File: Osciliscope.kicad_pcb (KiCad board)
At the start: 2 copper layers, 39.6 x 60.2 mm, 42 parts, among them J1 U.FL, J2 Conn_01x04_Socket, J3 U.FL, J4 Conn_01x04_Socket, J5 USB_C_Receptacle_USB2.0_14P, J6 Conn_01x02_MountingPin, SW1 SW_Rotary_1x8_MP, SW2 SW_Rotary_1x8_MP, SW3 SW_Nidec_CAS-120A1, SW4 SW_Nidec_CAS-120A1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

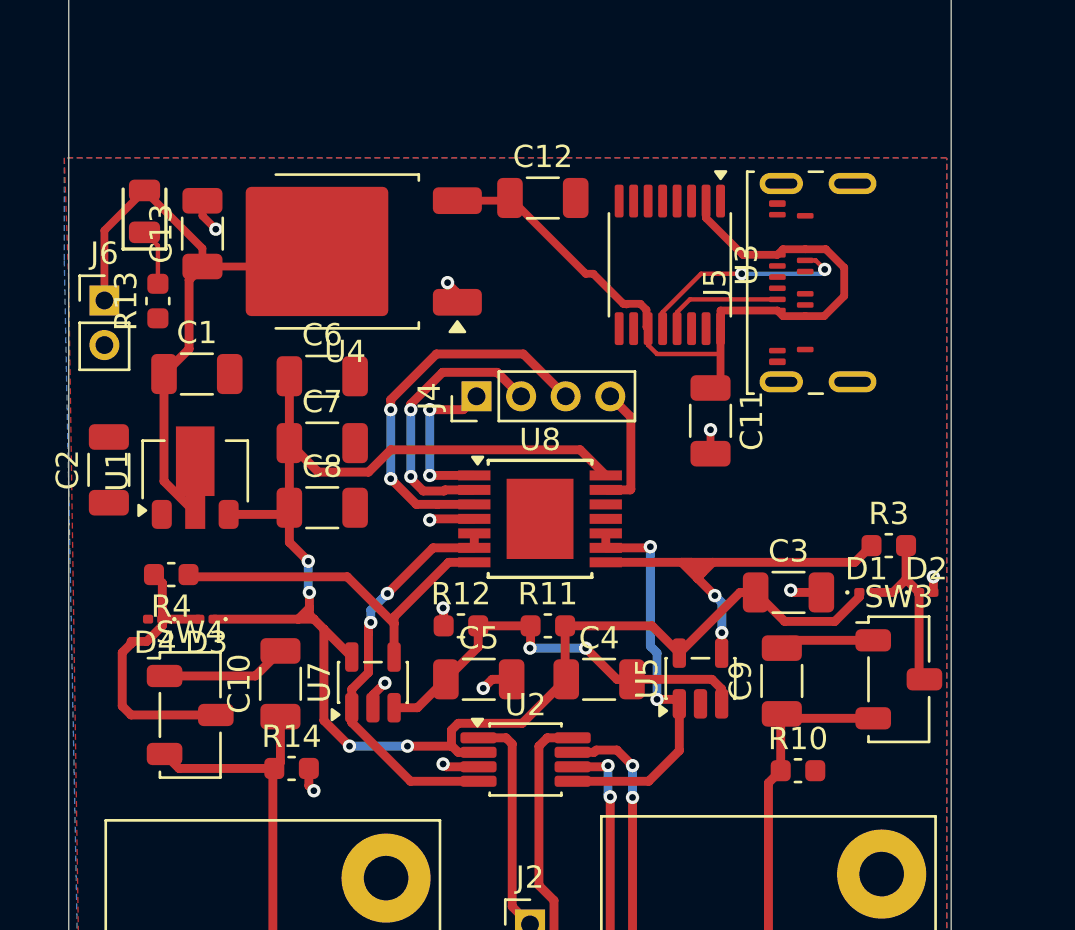
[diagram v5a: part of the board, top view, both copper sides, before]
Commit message: Reorient film mask
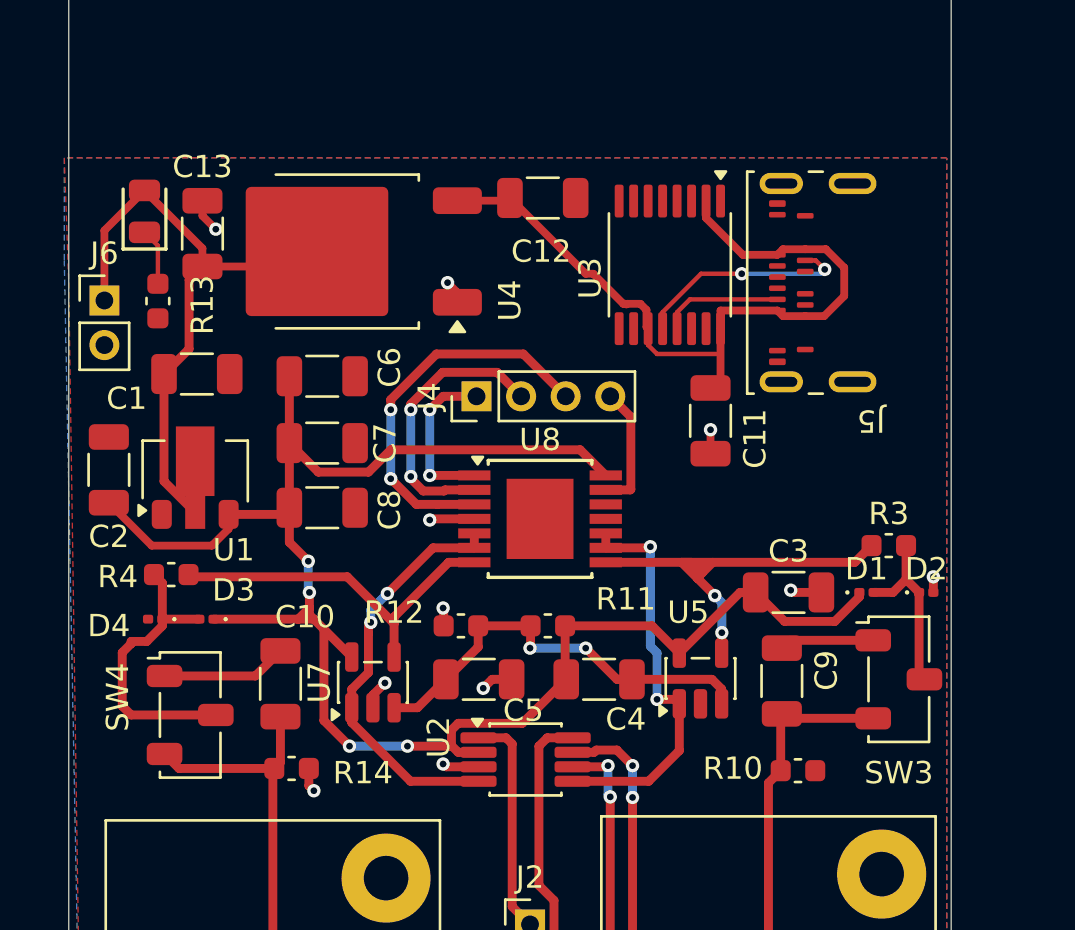
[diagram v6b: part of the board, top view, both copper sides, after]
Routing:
- net V3.3: track 74.4 -> 81.5 mm
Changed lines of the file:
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@@
 		(tags "USB C Type-C Waterproof")
 		(property "Reference" "J5"
-			(at 0 -6 90)
+			(at -6.2 1 180)
 			(unlocked yes)
 			(layer "F.SilkS")
@@
 		(tags "capacitor")
 		(property "Reference" "R12"
-			(at 0 -1.43 0)
+			(at -3 -0.6 0)
 			(layer "F.SilkS")
 			(effects
@@
 		(tags "capacitor")
 		(property "Reference" "R13"
-			(at 0 -1.43 90)
+			(at -0.175 2 90)
 			(layer "F.SilkS")
 			(effects
@@
 		(tags "capacitor")
 		(property "Reference" "C7"
-			(at 0 -1.85 0)
+			(at 2.825 0 90)
 			(layer "F.SilkS")
 			(effects
@@
 		(tags "TSSOP SO JEDEC-MO-153-AB Texas_PW0016A Microchip-ST Toshiba-TSSOP16-P-0044-0.65A NXP-SOT403-1 Infineon-P-TSSOP-16-800")
 		(property "Reference" "U3"
-			(at 0 -3.449999 90)
+			(at 0.6 3.575 90)
 			(layer "F.SilkS")
 			(effects
@@
 		(tags "DPAK TO-252 DPAK-3 TO-252-3 SOT-428")
 		(property "Reference" "U4"
-			(at 0 -4.500001 0)
+			(at -7.4 -2.2 90)
 			(layer "F.SilkS")
 			(effects
@@
 		(tags "capacitor")
 		(property "Reference" "C1"
-			(at 0 -1.85 0)
+			(at -3.15 1.1 0)
 			(layer "F.SilkS")
 			(effects
@@
 		(tags "capacitor")
 		(property "Reference" "R4"
-			(at 0 -1.43 0)
+			(at 2.4 -0.1 0)
 			(layer "F.SilkS")
 			(effects
@@
 		(tags "capacitor")
 		(property "Reference" "C5"
-			(at 0 -1.85 0)
+			(at 2 1.4 0)
 			(layer "F.SilkS")
 			(effects
@@
 		(tags "capacitor")
 		(property "Reference" "C12"
-			(at 0 -1.850001 0)
+			(at -0.075001 2.4 0)
 			(layer "F.SilkS")
 			(effects
@@
 		(tags "capacitor")
 		(property "Reference" "C8"
-			(at 0 -1.85 0)
+			(at 3.025 0.1 90)
 			(layer "F.SilkS")
 			(effects
@@
 		(tags "capacitor")
 		(property "Reference" "R10"
-			(at 0 -1.43 0)
+			(at -2.925 -0.1 0)
 			(layer "F.SilkS")
 			(effects
@@
 		(tags "capacitor")
 		(property "Reference" "C10"
-			(at 0 -1.85 90)
+			(at 3 1.1 180)
 			(layer "F.SilkS")
 			(effects
@@
 		(tags "SOT TO_SOT_SMD")
 		(property "Reference" "U5"
-			(at 0 -2.4 90)
+			(at 2.9625 -0.55 180)
 			(layer "F.SilkS")
 			(effects
@@
 		(tags "capacitor")
 		(property "Reference" "C11"
-			(at 0 -1.850001 90)
+			(at 0.8 -2 90)
 			(layer "F.SilkS")
 			(effects
@@
 		(tags "capacitor")
 		(property "Reference" "C4"
-			(at 0 -1.85 0)
+			(at 1.2 1.8 0)
 			(layer "F.SilkS")
 			(effects
@@
 		(tags "SMD slide switch Nidec CAS 120A ")
 		(property "Reference" "SW3"
-			(at 0 -3.7 0)
+			(at 0 4.2 0)
 			(unlocked yes)
 			(layer "F.SilkS")
@@
 		(tags "diode")
 		(property "Reference" "D4"
-			(at 0 -1.05 0)
+			(at 2.08 -0.3 0)
 			(layer "F.SilkS")
 			(effects
@@
 		(tags "capacitor")
 		(property "Reference" "C13"
-			(at 0 -1.850001 90)
+			(at 3 0 180)
 			(layer "F.SilkS")
 			(effects
@@
 		(tags "SOT-89-3")
 		(property "Reference" "U1"
-			(at 0 -3.5 90)
+			(at -3.55 1.725 180)
 			(layer "F.SilkS")
 			(effects
@@
 		(tags "capacitor")
 		(property "Reference" "C9"
-			(at 0 -1.85 90)
+			(at 0.475 2 90)
 			(layer "F.SilkS")
 			(effects
@@
 		(tags "capacitor")
 		(property "Reference" "R14"
-			(at 0 -1.43 0)
+			(at 3.2 0.2 0)
 			(layer "F.SilkS")
 			(effects
@@
 		(tags "capacitor")
 		(property "Reference" "C6"
-			(at 0 -1.85 0)
+			(at 3.025 -0.4 90)
 			(layer "F.SilkS")
 			(effects
@@
 		(tags "capacitor")
 		(property "Reference" "C2"
-			(at 0 -1.850001 90)
+			(at -3 0 180)
 			(layer "F.SilkS")
 			(effects
@@
 		(tags "VSSOP SO JEDEC-MO-187-AA Texas_DGK0008A")
 		(property "Reference" "U2"
-			(at 0 -2.45 0)
+			(at -3.9 -1 90)
 			(layer "F.SilkS")
 			(effects
@@
 		(tags "capacitor")
 		(property "Reference" "R11"
-			(at 0 -1.43 0)
+			(at 3.5 -1.2 0)
 			(layer "F.SilkS")
 			(effects
@@
 		(tags "diode")
 		(property "Reference" "D3"
-			(at 0 -1.05 0)
+			(at -1.22 1.3 0)
 			(layer "F.SilkS")
 			(effects
@@
 		(tags "SMD slide switch Nidec CAS 120A ")
 		(property "Reference" "SW4"
-			(at 0 -3.7 0)
+			(at -3.25 -0.8 90)
 			(unlocked yes)
 			(layer "F.SilkS")
@@
 	)
 	(segment
+		(start 92.025 150.8)
+		(end 92.775 150.05)
+		(width 0.35)
+		(layer "F.Cu")
+		(net 14)
+	)
+	(segment
 		(start 97.05 154.55)
 		(end 96.6 154.1)
@@
 	)
 	(segment
+		(start 89.324999 150.8)
+		(end 92.025 150.8)
+		(width 0.35)
+		(layer "F.Cu")
+		(net 14)
+	)
+	(segment
 		(start 92.775 149.4)
 		(end 95.2 149.4)
@@
 	)
 	(segment
+		(start 92.775 150.05)
+		(end 92.775 149.4)
+		(width 0.35)
+		(layer "F.Cu")
+		(net 14)
+	)
+	(segment
 		(start 103.07766 160.075)
 		(end 103.9875 160.075)
@@
 	)
 	(segment
+		(start 87.4 148.875001)
+		(end 89.324999 150.8)
+		(width 0.35)
+		(layer "F.Cu")
+		(net 14)
+	)
+	(segment
 		(start 100.8 159.8)
 		(end 102.74534 159.8)
@@
 	)
 	(segment
-		(start 101.8 144.7)
-		(end 103.3 144.7)
+		(start 102.4 144.1)
+		(end 103.9 144.1)
 		(width 0.4)
 		(layer "F.Cu")
@@
 	)
 	(segment
-		(start 103.3 144.7)
-		(end 103.9 144.1)
+		(start 101.8 144.7)
+		(end 102.4 144.1)
 		(width 0.4)
 		(layer "F.Cu")

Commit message: Improvment
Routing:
- net GND: track 14.1 -> 27.7 mm, vias 11 -> 12
- net 5Vin: track 28.1 -> 23.6 mm
- net USBCRAW: track 35.9 -> 36.8 mm
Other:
- board text added: "DESIGNED BY: Ethan Marreel Jordan ___ Daniel ___"
- board text added: "OPEN OSCILISCOPE JD 2"
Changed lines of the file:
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@@
 		)
 		(fp_text user "Keep out zone"
-			(at 0 5 90)
+			(at 0 2.8 90)
 			(unlocked yes)
 			(layer "Cmts.User")
@@
 	)
 	(gr_rect
+		(start 91.6 137.8)
+		(end 94.4 138.8)
+		(stroke
+			(width 0.2)
+			(type solid)
+		)
+		(fill yes)
+		(layer "F.Cu")
+		(net 1)
+	)
+	(gr_rect
 		(start 85.6 119.8)
 		(end 125.2 180)
@@
 		(layer "Edge.Cuts")
 	)
+	(gr_text "DESIGNED BY:\nEthan Marreel\nJordan ___\nDaniel ___"
+		(at 113.8 126.4 0)
+		(layer "F.SilkS")
+		(effects
+			(font
+				(size 1 1)
+				(thickness 0.2)
+				(bold yes)
+			)
+			(justify left bottom)
+		)
+	)
+	(gr_text "OPEN OSCILISCOPE\nJD 2\n"
+		(at 86.2 124.6 0)
+		(layer "F.SilkS")
+		(effects
+			(font
+				(size 1.5 1.5)
+				(thickness 0.3)
+				(bold yes)
+			)
+			(justify left bottom)
+		)
+	)
 	(segment
 		(start 89.875 143.1)
-		(end 91 141.975)
+		(end 91.6 141.375)
 		(width 0.4)
 		(layer "F.Cu")
@@
 		(start 89 134.860001)
 		(end 91.6 137.460001)
-		(width 0.35)
+		(width 0.5)
 		(layer "F.Cu")
 		(net 1)
 	)
 	(segment
-		(start 91 141.975)
-		(end 91 138.875001)
+		(start 91.6 141.375)
+		(end 91.6 138.275001)
 		(width 0.4)
 		(layer "F.Cu")
@@
 	)
 	(segment
+		(start 87.2 136.660001)
+		(end 89 134.860001)
+		(width 0.5)
+		(layer "F.Cu")
+		(net 1)
+	)
+	(segment
 		(start 89.875 143.1)
 		(end 89.875 147.9125)
@@
 	)
 	(segment
-		(start 87.2 136.660001)
-		(end 89 134.860001)
-		(width 0.35)
-		(layer "F.Cu")
-		(net 1)
-	)
-	(segment
 		(start 89.875 147.9125)
 		(end 91.275 149.3125)
@@
 	)
 	(segment
-		(start 87.2 139.8)
-		(end 87.2 136.660001)
-		(width 0.35)
-		(layer "F.Cu")
-		(net 1)
-	)
-	(segment
-		(start 91.6 138.275001)
-		(end 96.064998 138.275001)
-		(width 0.35)
-		(layer "F.Cu")
-		(net 1)
-	)
-	(segment
 		(start 91.6 137.460001)
 		(end 91.6 138.275001)
-		(width 0.35)
+		(width 0.5)
 		(layer "F.Cu")
 		(net 1)
 	)
 	(segment
-		(start 91 138.875001)
-		(end 91.6 138.275001)
-		(width 0.4)
+		(start 87.2 139.8)
+		(end 87.2 136.660001)
+		(width 0.5)
 		(layer "F.Cu")
 		(net 1)
@@
 	)
 	(segment
+		(start 112.25 136.95)
+		(end 112.2 137)
+		(width 0.35)
+		(layer "F.Cu")
+		(net 9)
+	)
+	(segment
 		(start 91.6 136)
 		(end 92.2 136.6)
@@
 	)
 	(segment
+		(start 117.4 142.05)
+		(end 117.4 143.275)
+		(width 0.35)
+		(layer "F.Cu")
+		(net 9)
+	)
+	(segment
 		(start 119.375 152.9)
 		(end 118.1 152.9)
@@
 	)
 	(segment
+		(start 118.65 136)
+		(end 117.45 136)
+		(width 0.35)
+		(layer "F.Cu")
+		(net 9)
+	)
+	(segment
+		(start 112.25 135.3375)
+		(end 112.25 136.95)
+		(width 0.35)
+		(layer "F.Cu")
+		(net 9)
+	)
+	(segment
 		(start 105.475 156.8)
 		(end 104.6 156.8)
@@
 	)
 	(segment
+		(start 117.45 136)
+		(end 117.4 135.95)
+		(width 0.35)
+		(layer "F.Cu")
+		(net 9)
+	)
+	(segment
+		(start 117.575 134.55)
+		(end 120.775 134.55)
+		(width 0.35)
+		(layer "F.Cu")
+		(net 9)
+	)
+	(segment
 		(start 96.375 161.575)
 		(end 96.6 161.8)
@@
 	)
 	(segment
+		(start 117.4 143.275)
+		(end 117.575 143.45)
+		(width 0.35)
+		(layer "F.Cu")
+		(net 9)
+	)
+	(segment
+		(start 117.4 134.725)
+		(end 117.575 134.55)
+		(width 0.35)
+		(layer "F.Cu")
+		(net 9)
+	)
+	(segment
 		(start 103.04 139.44)
 		(end 102.6 139)
@@
 	)
 	(segment
+		(start 117.45 142)
+		(end 117.4 142.05)
+		(width 0.35)
+		(layer "F.Cu")
+		(net 9)
+	)
+	(segment
 		(start 104.6 156.8)
 		(end 104.2 157.2)
@@
 	)
 	(segment
+		(start 117.575 143.45)
+		(end 120.775 143.45)
+		(width 0.35)
+		(layer "F.Cu")
+		(net 9)
+	)
+	(segment
 		(start 102.425 154.4)
 		(end 102.425 153.625)
@@
 	)
 	(segment
+		(start 118.65 142)
+		(end 117.45 142)
+		(width 0.35)
+		(layer "F.Cu")
+		(net 9)
+	)
+	(segment
 		(start 102.525 160.725)
 		(end 102.4 160.6)
@@
 		(net 9)
 	)
+	(segment
+		(start 117.4 135.95)
+		(end 117.4 134.725)
+		(width 0.35)
+		(layer "F.Cu")
+		(net 9)
+	)
 	(via
 		(at 114.4 145.6)
@@
 	)
 	(via
+		(at 112.2 137)
+		(size 0.6)
+		(drill 0.3)
+		(layers "F.Cu" "B.Cu")
+		(net 9)
+	)
+	(via
 		(at 102.4 160.6)
 		(size 0.6)
@@
 	)
 	(segment
-		(start 112.000001 142.2)
-		(end 114.85 142.2)
-		(width 0.2)
+		(start 110.625 139.974062)
+		(end 110.650062 139.949)
+		(width 0.35)
 		(layer "F.Cu")
 		(net 40)
 	)
 	(segment
-		(start 110.625 139.974062)
-		(end 110.650062 139.949)
+		(start 111.6 141.825938)
+		(end 111.6 141.0625)
 		(width 0.35)
 		(layer "F.Cu")
@@
 	)
 	(segment
+		(start 114.4 143.724999)
+		(end 113.499061 143.724999)
+		(width 0.35)
+		(layer "F.Cu")
+		(net 40)
+	)
+	(segment
 		(start 108.8 138.6)
 		(end 109.1375 138.6)
@@
 	)
 	(segment
+		(start 113.499061 143.724999)
+		(end 111.6 141.825938)
+		(width 0.35)
+		(layer "F.Cu")
+		(net 40)
+	)
+	(segment
 		(start 110.599938 139.949)
 		(end 110.625 139.974062)
@@
 		(layer "F.Cu")
 		(net 40)
-	)
-	(segment
-		(start 111.6 141.799999)
-		(end 112.000001 142.2)
-		(width 0.2)
-		(layer "F.Cu")
-		(net 40)

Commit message: more small changes
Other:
- board text added: "DESIGNED BY: Ethan Marreel Jordan Savin Daniel Stucker"
- board text removed: "DESIGNED BY: Ethan Marreel Jordan ___ Daniel ___"
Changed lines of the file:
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@@
 		(layer "Edge.Cuts")
 	)
-	(gr_text "DESIGNED BY:\nEthan Marreel\nJordan ___\nDaniel ___"
+	(gr_text "DESIGNED BY:\nEthan Marreel\nJordan Savin\nDaniel Stucker"
 		(at 113.8 126.4 0)
 		(layer "F.SilkS")
